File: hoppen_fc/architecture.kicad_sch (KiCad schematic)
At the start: 0 parts

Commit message: work
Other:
- added sheet Power Generation (power_generation.kicad_sch)
- added sheet Power Input (power_input.kicad_sch)
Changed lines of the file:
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@@
+	)
+	(sheet
+		(at 38.1 95.25)
+		(size 12.7 3.81)
+		(exclude_from_sim no)
+		(in_bom yes)
+		(on_board yes)
+		(dnp no)
+		(fields_autoplaced yes)
+		(stroke
+			(width 0.1524)
+			(type solid)
+		)
+		(fill
+			(color 0 0 0 0.0000)
+		)
+		(property "Sheetname" "Power Generation"
+			(at 38.1 94.5384 0)
+			(effects
+				(font
+					(size 1.27 1.27)
+				)
+				(justify left bottom)
+			)
+		)
+		(property "Sheetfile" "power_generation.kicad_sch"
+			(at 38.1 99.6446 0)
+			(effects
+				(font
+					(size 1.27 1.27)
+				)
+				(justify left top)
+			)
+		)
+		(instances
+			(project "hoppen_fc"
+				(path "/abe950a1-9eef-4508-9fd4-31d3e723e029/c85454e5-a89e-41eb-a5ed-71b4fc4cf13a"
+					(page "16")
+				)
+			)
+		)
 	)
 	(sheet
@@
 				)
 			)
+		)
+	)
+	(sheet
+		(at 35.56 69.85)
+		(size 12.7 3.81)
+		(exclude_from_sim no)
+		(in_bom yes)
+		(on_board yes)
+		(dnp no)
+		(fields_autoplaced yes)
+		(stroke
+			(width 0.1524)
+			(type solid)
+		)
+		(fill
+			(color 0 0 0 0.0000)
+		)
+		(property "Sheetname" "Power Input"
+			(at 35.56 69.1384 0)
+			(effects
+				(font
+					(size 1.27 1.27)
+				)
+				(justify left bottom)
+			)
+		)
+		(property "Sheetfile" "power_input.kicad_sch"
+			(at 35.56 74.2446 0)
+			(effects
+				(font
+					(size 1.27 1.27)
+				)
+				(justify left top)
+			)
+		)
+		(instances
+			(project "hoppen_fc"
+				(path "/abe950a1-9eef-4508-9fd4-31d3e723e029/c85454e5-a89e-41eb-a5ed-71b4fc4cf13a"
+					(page "15")
+				)
+			)

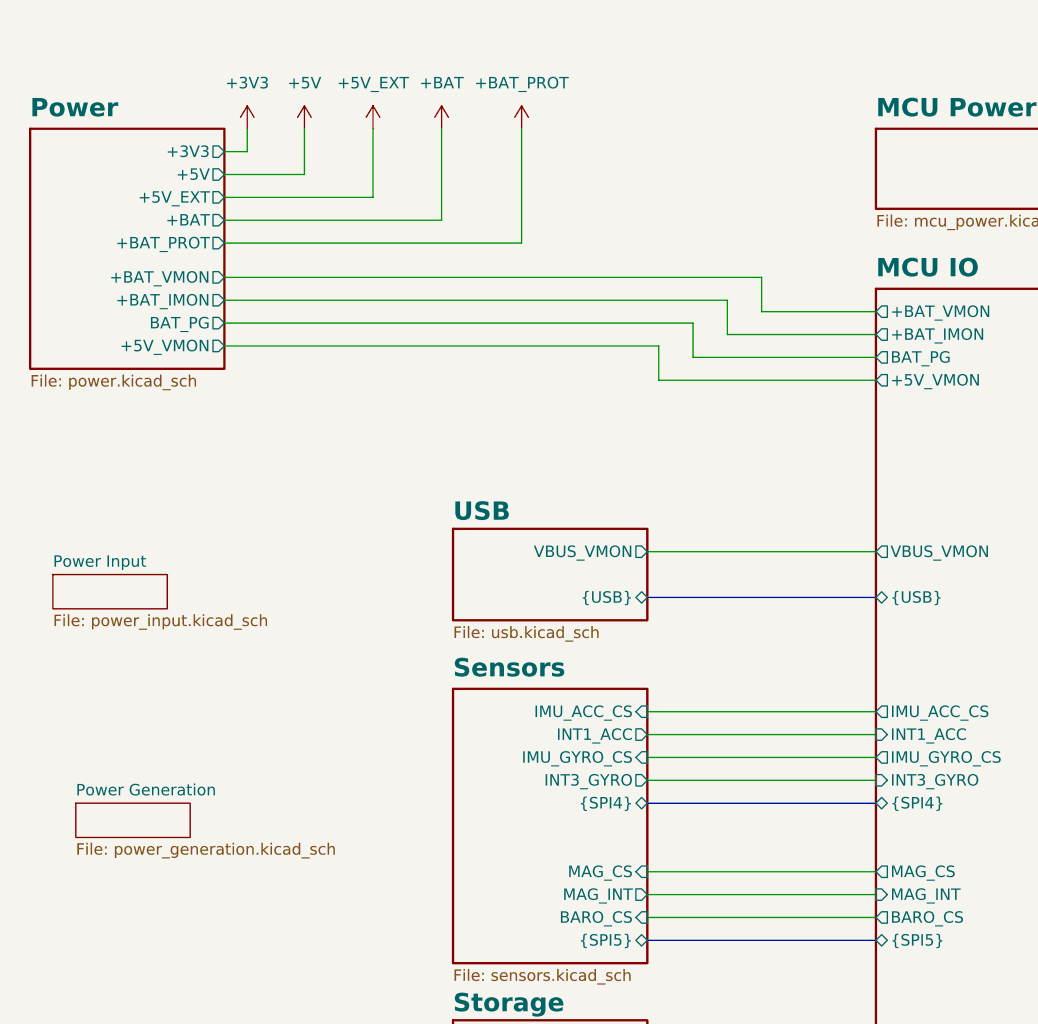
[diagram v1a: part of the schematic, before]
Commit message: power input/generation reworked
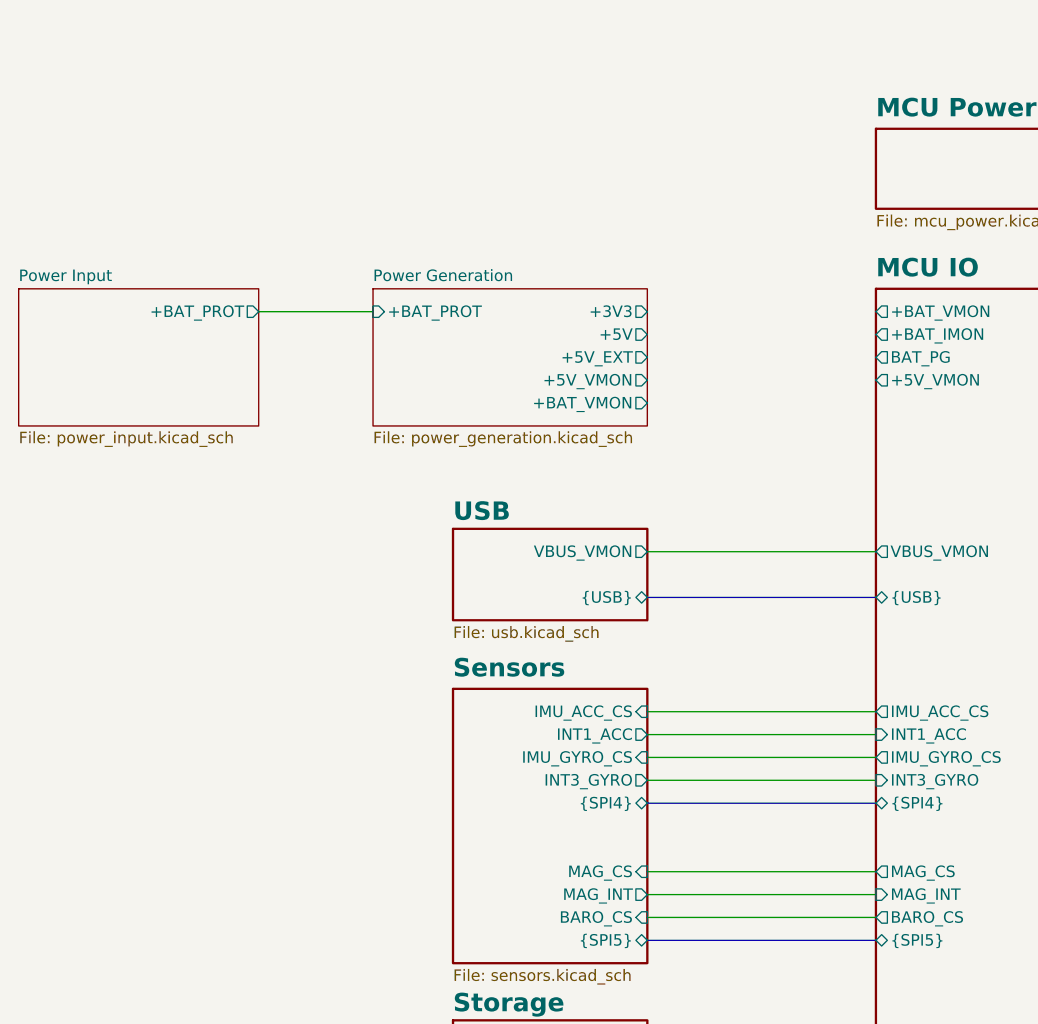
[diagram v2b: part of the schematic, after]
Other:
- removed sheet Power
- sheet Power Generation ports: added +3V3, +5V, +5V_EXT, +5V_VMON, +BAT_PROT, +BAT_VMON; removed none
- sheet Power Input ports: added +BAT_PROT; removed none

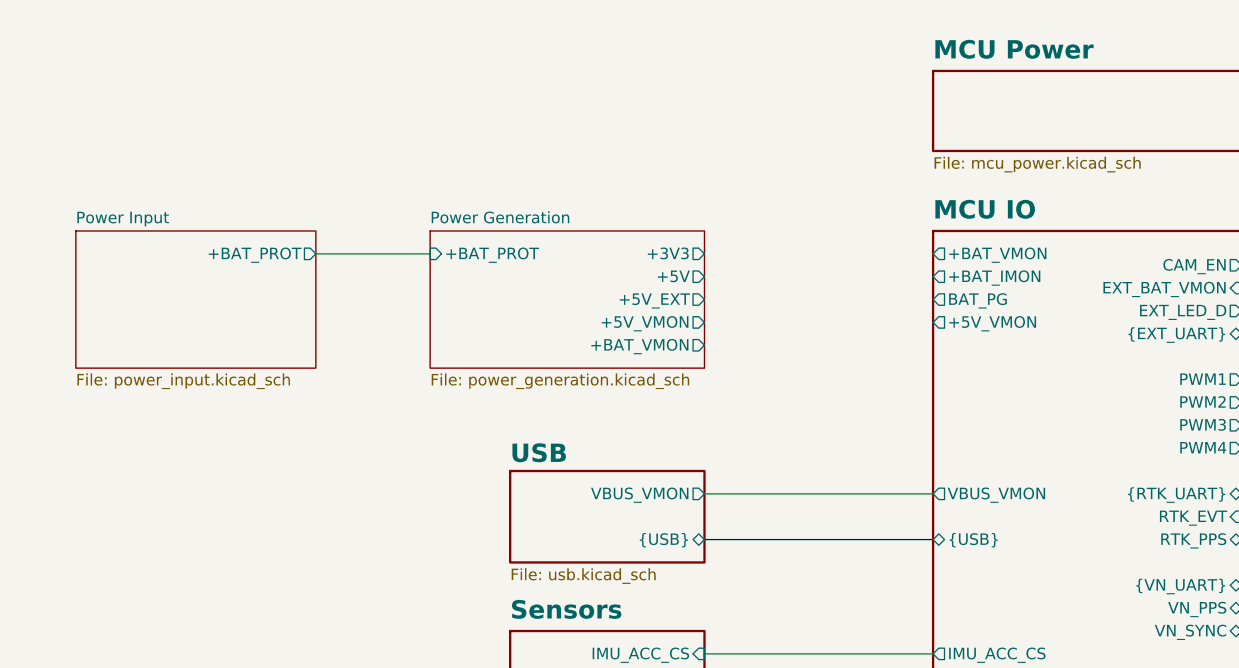
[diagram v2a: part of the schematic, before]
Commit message: finished adding lcsc numbers
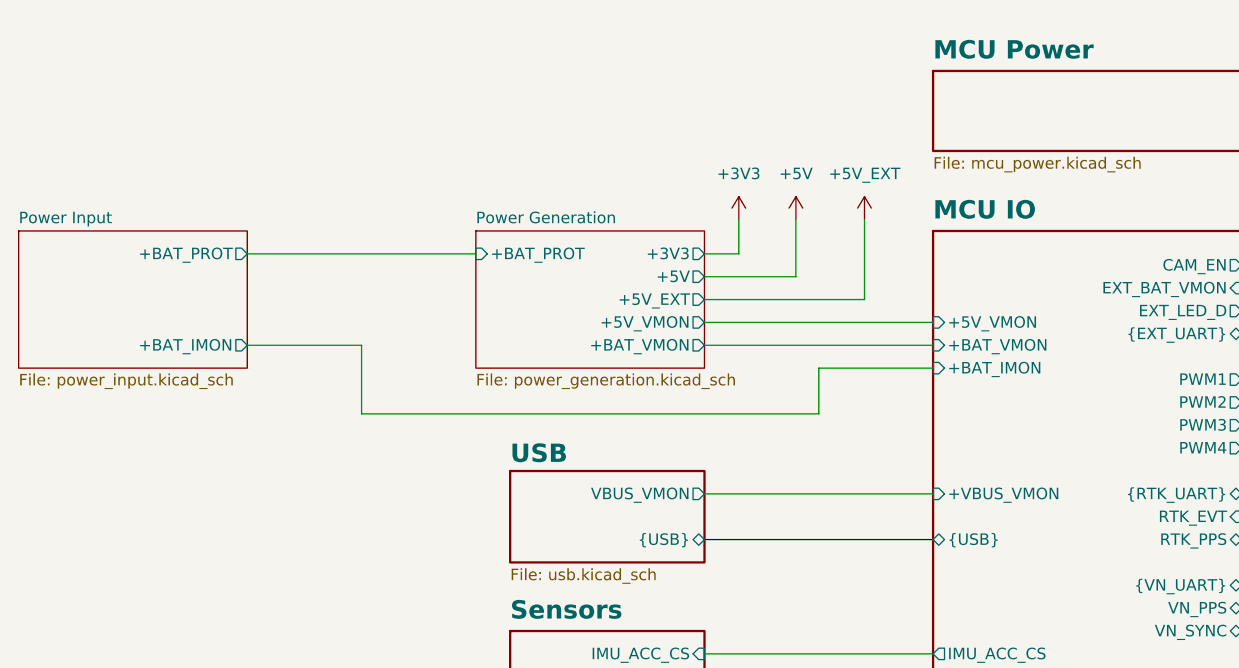
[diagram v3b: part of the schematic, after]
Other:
- sheet MCU IO ports: added +VBUS_VMON; removed BAT_PG, VBUS_VMON
- sheet Power Input ports: added +BAT_IMON; removed none

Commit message: ready for routing?
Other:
- sheet MCU IO ports: added none; removed RS232_nEN, RS232_nSHDN
- sheet RS232 ports: added none; removed RS232_nEN, RS232_nSHDN
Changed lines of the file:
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@@
-	(wire
-		(pts
-			(xy 161.29 118.11) (xy 175.26 118.11)
-		)
-		(stroke
-			(width 0)
-			(type default)
-		)
-	)
 	(wire
 		(pts
@@
 	(wire
 		(pts
+			(xy 50.8 40.64) (xy 73.66 40.64)
+		)
+		(stroke
+			(width 0)
+			(type default)
+		)
+	)
+	(wire
+		(pts
 			(xy 105.41 40.64) (xy 105.41 36.83)
 		)
@@
 		)
 	)
-	(wire
-		(pts
-			(xy 50.8 40.64) (xy 76.2 40.64)
-		)
-		(stroke
-			(width 0)
-			(type default)
-		)
-	)
 	(bus
 		(pts
@@
 		(pts
 			(xy 212.09 107.95) (xy 212.09 77.47)
-		)
-		(stroke
-			(width 0)
-			(type default)
-		)
-	)
-	(wire
-		(pts
-			(xy 161.29 113.03) (xy 175.26 113.03)
 		)
 		(stroke
@@
 	)
 	(sheet
-		(at 76.2 38.1)
-		(size 25.4 15.24)
+		(at 73.66 38.1)
+		(size 27.94 15.24)
 		(exclude_from_sim no)
 		(in_bom yes)
@@
 		)
 		(property "Sheetname" "Power Generation"
-			(at 76.2 37.3884 0)
-			(effects
-				(font
-					(size 1.27 1.27)
+			(at 73.66 37.0074 0)
+			(effects
+				(font
+					(size 2.032 2.032)
+					(thickness 0.4064)
+					(bold yes)
 				)
 				(justify left bottom)
@@
 		)
 		(property "Sheetfile" "power_generation.kicad_sch"
-			(at 76.2 53.9246 0)
+			(at 73.66 53.9246 0)
 			(effects
 				(font
@@
 		)
 		(pin "+BAT_PROT" input
-			(at 76.2 40.64 180)
+			(at 73.66 40.64 180)
 			(effects
 				(font
@@
 		)
 		(property "Sheetname" "Power Input"
-			(at 25.4 37.3884 0)
-			(effects
-				(font
-					(size 1.27 1.27)
+			(at 25.4 37.0074 0)
+			(effects
+				(font
+					(size 2.032 2.032)
+					(thickness 0.4064)
+					(bold yes)
 				)
 				(justify left bottom)
@@
 			)
 		)
-		(pin "RS232_nEN" input
-			(at 175.26 118.11 180)
-			(effects
-				(font
-					(size 1.27 1.27)
-				)
-				(justify left)
-			)
-		)
-		(pin "RS232_nSHDN" input
-			(at 175.26 113.03 180)
-			(effects
-				(font
-					(size 1.27 1.27)
-				)
-				(justify left)
-			)
-		)
 		(pin "{RS232_IN}" bidirectional
 			(at 175.26 107.95 180)
@@
 			(effects
 				(font
-					(size 1.27 1.27)
-				)
-				(justify right)
-			)
-		)
-		(pin "RS232_nEN" output
-			(at 161.29 118.11 0)
-			(effects
-				(font
-					(size 1.27 1.27)
-				)
-				(justify right)
-			)
-		)
-		(pin "RS232_nSHDN" output
-			(at 161.29 113.03 0)
-			(effects
-				(font

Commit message: routing and adding rf module
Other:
- added sheet Radio (radio.kicad_sch)
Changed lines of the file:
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@@
+	)
+	(sheet
+		(at 175.26 147.32)
+		(size 27.94 10.16)
+		(exclude_from_sim no)
+		(in_bom yes)
+		(on_board yes)
+		(dnp no)
+		(fields_autoplaced yes)
+		(stroke
+			(width 0.1524)
+			(type solid)
+		)
+		(fill
+			(color 0 0 0 0.0000)
+		)
+		(property "Sheetname" "Radio"
+			(at 175.26 146.2274 0)
+			(effects
+				(font
+					(size 2.032 2.032)
+					(thickness 0.4064)
+					(bold yes)
+				)
+				(justify left bottom)
+			)
+		)
+		(property "Sheetfile" "radio.kicad_sch"
+			(at 175.26 158.0646 0)
+			(effects
+				(font
+					(size 1.27 1.27)
+				)
+				(justify left top)
+			)
+		)
+		(instances
+			(project "hoppen_fc"
+				(path "/abe950a1-9eef-4508-9fd4-31d3e723e029/c85454e5-a89e-41eb-a5ed-71b4fc4cf13a"
+					(page "15")
+				)
+			)
+		)
 	)
 	(sheet

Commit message: sync
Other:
- sheet MCU IO ports: added RADIO_CS, RADIO_DIO0, RADIO_DIO1, RADIO_DIO5, RADIO_RST, {SPI3}; removed none
- sheet Radio ports: added RADIO_CS, RADIO_DIO0, RADIO_DIO1, RADIO_DIO5, RADIO_RST, {SPI3}; removed none
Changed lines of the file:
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@@
+		)
+	)
+	(bus
+		(pts
+			(xy 161.29 123.19) (xy 175.26 123.19)
+		)
+		(stroke
+			(width 0)
+			(type default)
 		)
 	)
@@
 		)
 	)
+	(bus
+		(pts
+			(xy 161.29 129.54) (xy 175.26 129.54)
+		)
+		(stroke
+			(width 0)
+			(type default)
+		)
+	)
 	(wire
 		(pts
@@
 		)
 	)
+	(wire
+		(pts
+			(xy 161.29 144.78) (xy 175.26 144.78)
+		)
+		(stroke
+			(width 0)
+			(type default)
+		)
+	)
 	(bus
 		(pts
@@
 	(bus
 		(pts
-			(xy 215.9 130.81) (xy 215.9 62.23)
+			(xy 215.9 123.19) (xy 215.9 62.23)
 		)
 		(stroke
@@
 		)
 	)
+	(wire
+		(pts
+			(xy 161.29 151.13) (xy 175.26 151.13)
+		)
+		(stroke
+			(width 0)
+			(type default)
+		)
+	)
+	(bus
+		(pts
+			(xy 161.29 142.24) (xy 175.26 142.24)
+		)
+		(stroke
+			(width 0)
+			(type default)
+		)
+	)
 	(bus
 		(pts
@@
 		)
 	)
+	(wire
+		(pts
+			(xy 161.29 153.67) (xy 175.26 153.67)
+		)
+		(stroke
+			(width 0)
+			(type default)
+		)
+	)
 	(bus
 		(pts
@@
 	(bus
 		(pts
-			(xy 219.71 137.16) (xy 219.71 54.61)
+			(xy 219.71 129.54) (xy 219.71 54.61)
 		)
 		(stroke
@@
 		)
 	)
+	(wire
+		(pts
+			(xy 161.29 158.75) (xy 175.26 158.75)
+		)
+		(stroke
+			(width 0)
+			(type default)
+		)
+	)
 	(bus
 		(pts
@@
 		)
 	)
+	(wire
+		(pts
+			(xy 161.29 148.59) (xy 175.26 148.59)
+		)
+		(stroke
+			(width 0)
+			(type default)
+		)
+	)
 	(bus
 		(pts
@@
 	(bus
 		(pts
-			(xy 203.2 137.16) (xy 219.71 137.16)
-		)
-		(stroke
-			(width 0)
-			(type default)
-		)
-	)
-	(bus
-		(pts
-			(xy 161.29 130.81) (xy 175.26 130.81)
+			(xy 203.2 129.54) (xy 219.71 129.54)
 		)
 		(stroke
@@
 	(bus
 		(pts
-			(xy 203.2 130.81) (xy 215.9 130.81)
+			(xy 203.2 123.19) (xy 215.9 123.19)
 		)
 		(stroke
@@
 		(pts
 			(xy 63.5 50.8) (xy 63.5 58.42)
-		)
-		(stroke
-			(width 0)
-			(type default)
-		)
-	)
-	(bus
-		(pts
-			(xy 161.29 137.16) (xy 175.26 137.16)
 		)
 		(stroke
@@
 	)
 	(sheet
-		(at 175.26 147.32)
-		(size 27.94 10.16)
+		(at 175.26 139.7)
+		(size 27.94 21.59)
 		(exclude_from_sim no)
 		(in_bom yes)
@@
 		)
 		(fill
-			(color 0 0 0 0.0000)
+			(color 132 0 0 1.0000)
 		)
 		(property "Sheetname" "Radio"
-			(at 175.26 146.2274 0)
+			(at 175.26 138.6074 0)
 			(effects
 				(font
@@
 		)
 		(property "Sheetfile" "radio.kicad_sch"
-			(at 175.26 158.0646 0)
+			(at 175.26 161.8746 0)
 			(effects
 				(font
@@
 				)
 				(justify left top)
+			)
+		)
+		(pin "RADIO_CS" input
+			(at 175.26 144.78 180)
+			(effects
+				(font
+					(size 1.27 1.27)
+				)
+				(justify left)
+			)
+		)
+		(pin "{SPI3}" bidirectional
+			(at 175.26 142.24 180)
+			(effects
+				(font
+					(size 1.27 1.27)
+				)
+				(justify left)
+			)
+		)
+		(pin "RADIO_RST" input
+			(at 175.26 158.75 180)
+			(effects
+				(font
+					(size 1.27 1.27)
+				)
+				(justify left)
+			)
+		)
+		(pin "RADIO_DIO0" bidirectional
+			(at 175.26 153.67 180)
+			(effects
+				(font
+					(size 1.27 1.27)
+				)
+				(justify left)
+			)
+		)
+		(pin "RADIO_DIO1" bidirectional
+			(at 175.26 151.13 180)
+			(effects
+				(font
+					(size 1.27 1.27)
+				)
+				(justify left)
+			)
+		)
+		(pin "RADIO_DIO5" bidirectional
+			(at 175.26 148.59 180)
+			(effects
+				(font
+					(size 1.27 1.27)
+				)
+				(justify left)
 			)
 		)
@@
 	)
 	(sheet
-		(at 175.26 128.27)
+		(at 175.26 120.65)
 		(size 27.94 11.43)
 		(exclude_from_sim no)
@@
 		)
 		(property "Sheetname" "FDCAN"
-			(at 175.26 127.5076 0)
+			(at 175.26 119.8876 0)
 			(effects
 				(font
@@
 		)
 		(property "Sheetfile" "canbus.kicad_sch"
-			(at 175.26 140.3354 0)
+			(at 175.26 132.7154 0)
 			(effects
 				(font
@@
 		)
 		(pin "{FDCAN1_TTL}" bidirectional
-			(at 175.26 130.81 180)
+			(at 175.26 123.19 180)
 			(effects
 				(font
@@
 		)
 		(pin "{FDCAN1}" bidirectional
-			(at 203.2 130.81 0)
+			(at 203.2 123.19 0)
 			(effects
 				(font
@@
 		)
 		(pin "{FDCAN2_TTL}" bidirectional
-			(at 175.26 137.16 180)
+			(at 175.26 129.54 180)
 			(effects
 				(font
@@
 		)
 		(pin "{FDCAN2}" bidirectional
-			(at 203.2 137.16 0)
+			(at 203.2 129.54 0)
 			(effects
 				(font
@@
 	)
 	(sheet
-		(at 127 168.91)
+		(at 127 172.72)
 		(size 34.29 12.7)
 		(exclude_from_sim no)
@@
 		)
 		(property "Sheetname" "Misc"
-			(at 127 167.7666 0)
+			(at 127 171.5766 0)
 			(effects
 				(font
@@
 		)
 		(property "Sheetfile" "misc.kicad_sch"
-			(at 127 182.2454 0)
+			(at 127 186.0554 0)
 			(effects
 				(font
@@
 			(project "hoppen_fc"
 				(path "/abe950a1-9eef-4508-9fd4-31d3e723e029/c85454e5-a89e-41eb-a5ed-71b4fc4cf13a"
-					(page "15")
+					(page "16")
 				)
 			)
@@
 	(sheet
 		(at 80.01 139.7)
-		(size 21.59 16.51)
+		(size 21.59 20.32)
 		(exclude_from_sim no)
 		(in_bom yes)
@@
 		)
 		(property "Sheetname" "Indicators"
-			(at 80.01 138.9376 0)
+			(at 80.01 138.5566 0)
 			(effects
 				(font
@@
 		)
 		(property "Sheetfile" "indicators.kicad_sch"
-			(at 80.01 156.8454 0)
+			(at 80.01 160.6554 0)
 			(effects
 				(font
@@
 	(sheet
 		(at 175.26 105.41)
-		(size 27.94 15.24)
+		(size 27.94 7.62)
 		(exclude_from_sim no)
 		(in_bom yes)
@@
 		)
 		(property "Sheetname" "RS232"
-			(at 175.26 104.6476 0)
+			(at 175.26 104.2666 0)
 			(effects
 				(font
@@
 		)
 		(property "Sheetfile" "rs232.kicad_sch"
-			(at 175.26 121.2854 0)
+			(at 175.26 113.6654 0)
 			(effects
 				(font
@@
 	(sheet
 		(at 127 38.1)
-		(size 34.29 119.38)
+		(size 34.29 124.46)
 		(exclude_from_sim no)
 		(in_bom yes)
@@
 		)
 		(property "Sheetfile" "mcu_io.kicad_sch"
-			(at 127 158.1154 0)
+			(at 127 163.1954 0)
 			(effects
 				(font
@@
 		)
 		(pin "{FDCAN1_TTL}" bidirectional
-			(at 161.29 130.81 0)
+			(at 161.29 123.19 0)
 			(effects
 				(font
@@
 		)
 		(pin "{FDCAN2_TTL}" bidirectional
-			(at 161.29 137.16 0)
+			(at 161.29 129.54 0)
 			(effects
 				(font
@@
 			)
 		)
+		(pin "RADIO_CS" output
+			(at 161.29 144.78 0)
+			(effects
+				(font
+					(size 1.27 1.27)
+				)
+				(justify right)
+			)
+		)
+		(pin "RADIO_DIO0" bidirectional
+			(at 161.29 153.67 0)
+			(effects
+				(font
+					(size 1.27 1.27)
+				)
+				(justify right)
+			)
+		)
+		(pin "RADIO_DIO1" bidirectional
+			(at 161.29 151.13 0)
+			(effects
+				(font
+					(size 1.27 1.27)
+				)
+				(justify right)
+			)
+		)
+		(pin "{SPI3}" bidirectional
+			(at 161.29 142.24 0)
+			(effects
+				(font
+					(size 1.27 1.27)
+				)
+				(justify right)
+			)
+		)
+		(pin "RADIO_RST" output
+			(at 161.29 158.75 0)
+			(effects
+				(font
+					(size 1.27 1.27)
+				)
+				(justify right)
+			)
+		)
+		(pin "RADIO_DIO5" bidirectional
+			(at 161.29 148.59 0)
+			(effects
+				(font
+					(size 1.27 1.27)
+				)
+				(justify right)
+			)
+		)

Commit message: bump
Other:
- removed sheet Interfaces
- added sheet Interfaces - Actuators (interfaces_actuators.kicad_sch)
- added sheet Interfaces - Comms (interfaces_comms.kicad_sch)
- added sheet Interfaces - Sensors (interfaces_sensors.kicad_sch)
- sheet MCU IO ports: added ESC_TX_1, ESC_TX_2; removed none

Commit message: bump
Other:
- sheet Interfaces - Actuators ports: added PWM5, PWM6; removed none
- sheet Interfaces - Comms ports: added none; removed CAM_EN
- sheet MCU IO ports: added PWM5, PWM6, RADIO_DIO2, {I2C}, {SPI1}, {SPI2}; removed +VBUS_VMON, CAM_EN, RADIO_DIO5, {SPI3}, {SPI5}
- sheet Radio ports: added RADIO_DIO2, {SPI2}; removed RADIO_DIO5, {SPI3}
- sheet Sensors ports: added {SPI1}; removed {SPI5}
- sheet Storage ports: added {I2C}; removed none
- sheet USB ports: added none; removed VBUS_VMON
